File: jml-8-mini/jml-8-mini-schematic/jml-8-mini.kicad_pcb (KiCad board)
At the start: 4 copper layers, 136.4 x 81.5 mm, 50 parts, among them J1 BarrelJack, J2 SIO CHB, J3 UART, J4 CTC Extra Lines, J5 Address Decoding, J6 Z80 Lines, SW1 Reset, SW2 Power, U1 Z80CPU, U10 74LS74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

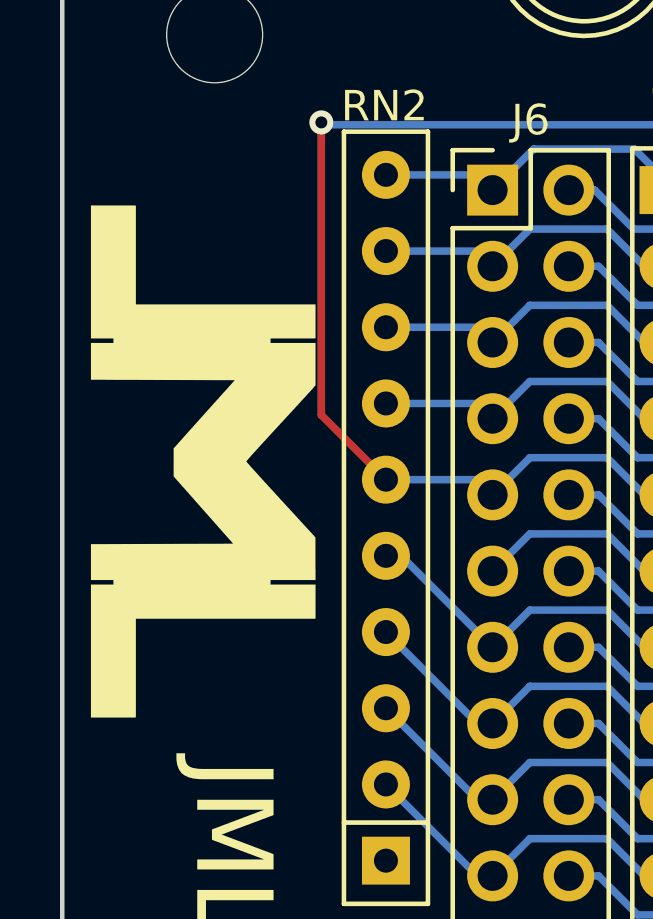
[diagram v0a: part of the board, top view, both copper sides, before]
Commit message: fix some errors in schematic/pcb
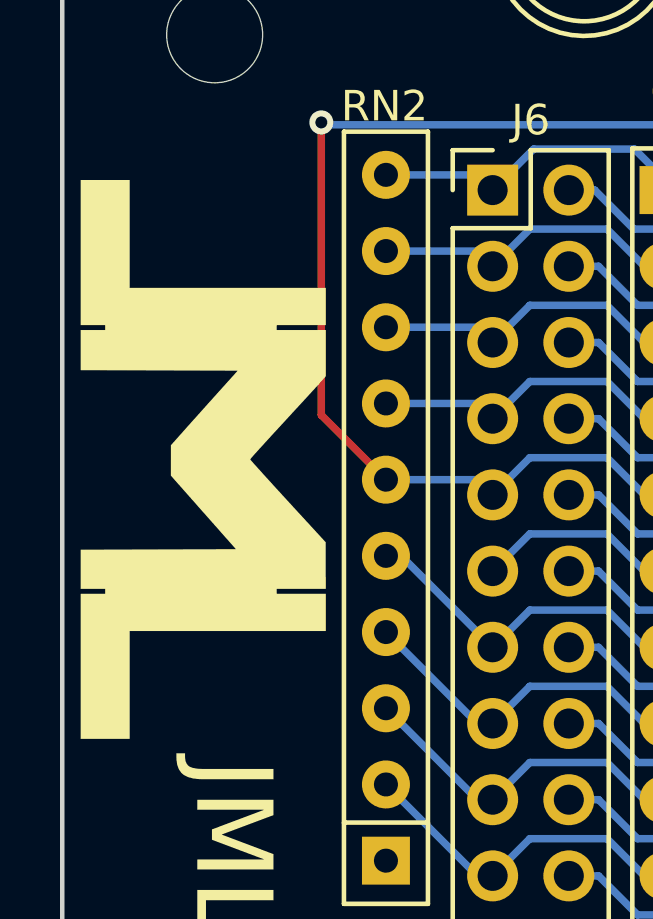
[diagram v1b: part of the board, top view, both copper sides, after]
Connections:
- J5 pad 11: /Address Decoding/Y2 -> /Address Decoding/Y1
- J5 pad 4: /Address Decoding/Y1 -> /Address Decoding/Y2
- U7 pad 10: /Address Decoding/Y1 -> /Address Decoding/Y2
- U7 pad 9: /Address Decoding/Y2 -> /Address Decoding/Y1
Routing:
- net /Address Decoding/Y2: track 27.0 -> 21.7 mm
- net /Address Decoding/Y1: track 21.7 -> 27.0 mm

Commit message: updates to silkscreen, regenerate gerbers
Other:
- board text added: "0"
- board text added: "11"
- board text added: "12"
- board text added: "13"
- board text added: "14"
- board text added: "15"
- board text added: "2"
- board text added: "3"
- board text added: "4"
- board text added: "5"
- board text added: "8"
- board text added: "9"
- board text added: "CLK1"
- board text added: "CLK2"
- board text added: "CLK3"
- board text added: "IEI"
- board text added: "IEO"
- board text added: "Q"
- board text added: "RxD"
- board text added: "TxD"
- board text added: "Y"
- board text added: "ZC1"
- board text added: "ZC2"
- board text added: "~{CTS}"
- board text added: "~{DCD}"
- board text added: "~{DTR}"
- board text added: "~{RTS}"
- board text added: "~{RxTxC}"
- board text added: "~{SYNC}"
- board text added: "~{W}/~{RDY}"
